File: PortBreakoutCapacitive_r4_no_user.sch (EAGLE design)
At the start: 10 parts, among them IC1 AT42QT1011-TSHR

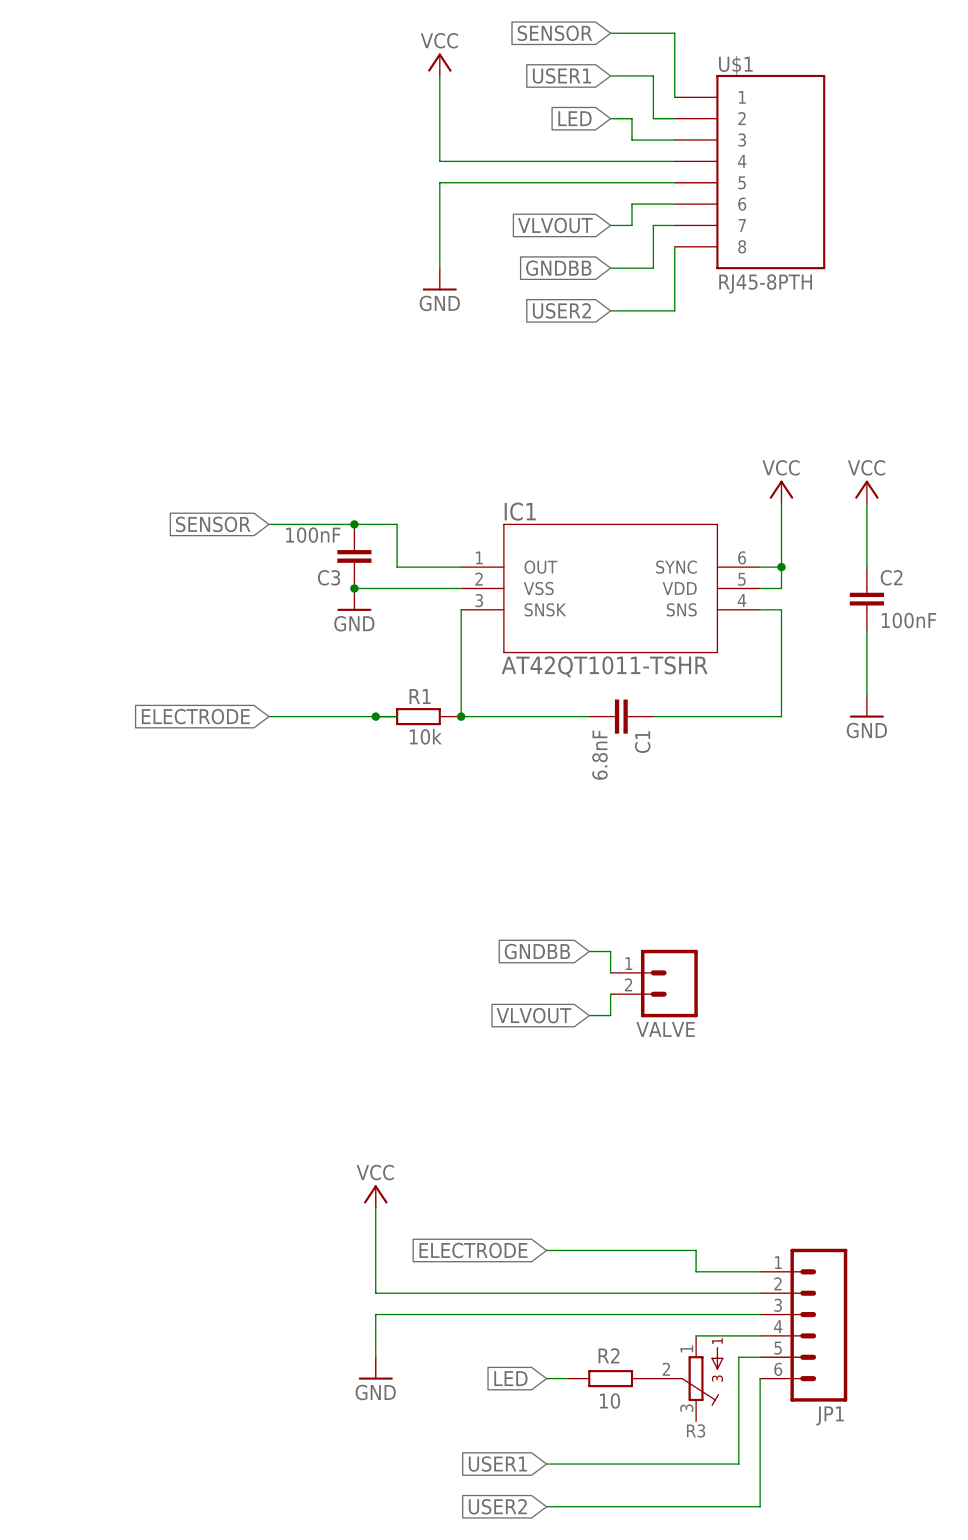
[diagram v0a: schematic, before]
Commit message: rev 4: C1 with lower capacitance
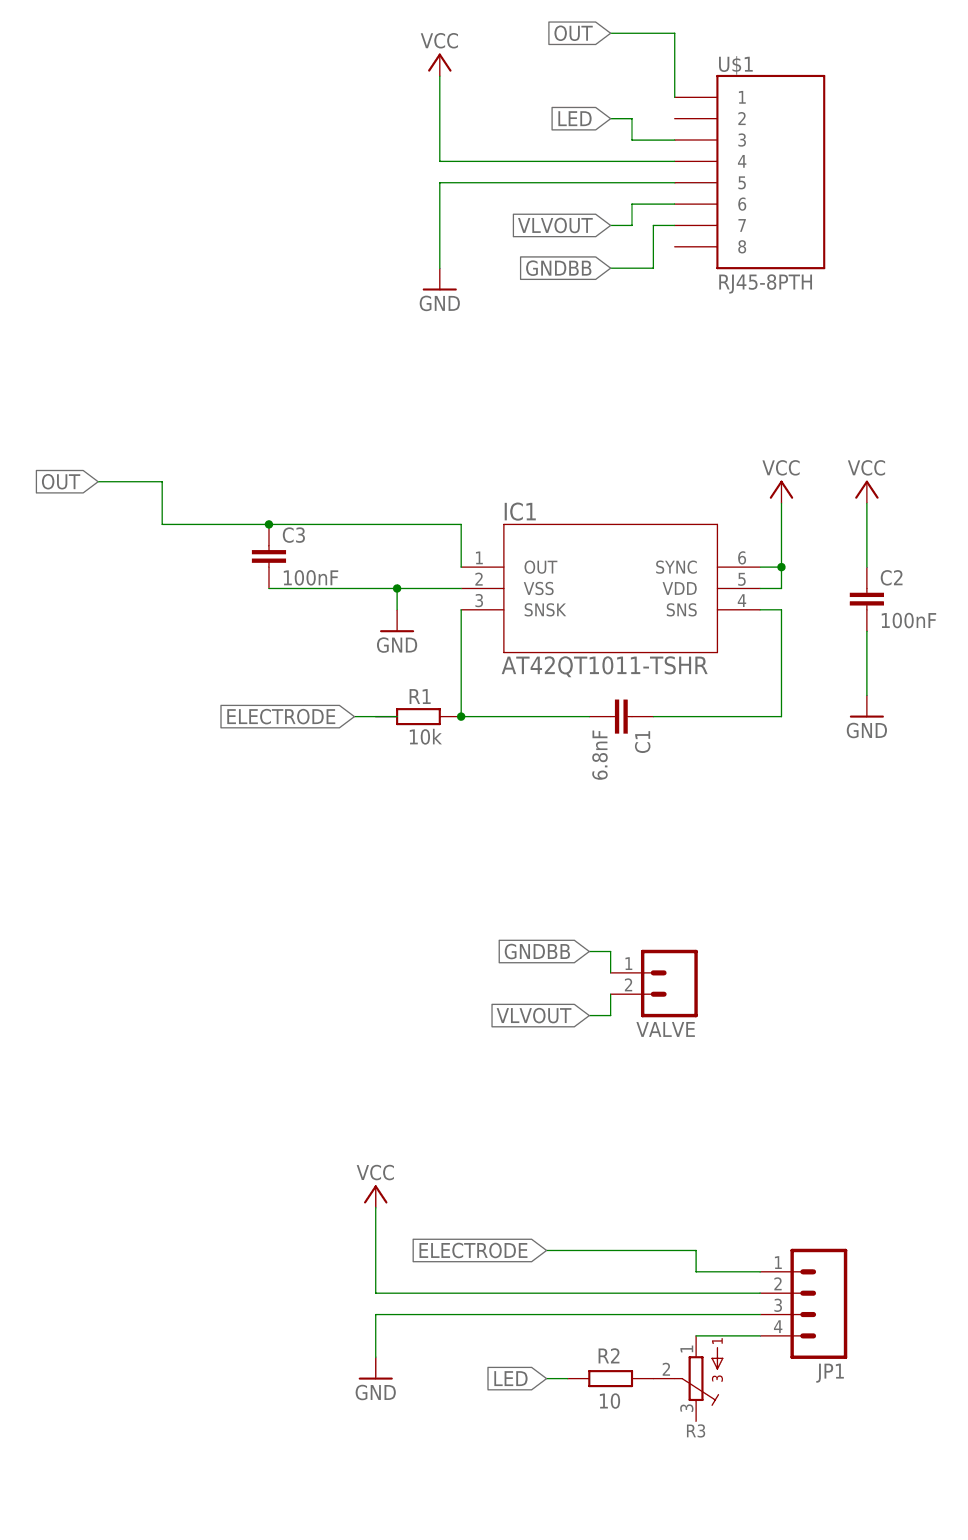
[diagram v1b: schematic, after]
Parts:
- JP1: device SparkFun:M063.5MM-6 -> SparkFun-Connectors:CONN_04SCREW
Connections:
- removed net SENSOR: C3.2, IC1.OUT, U$1.1
- removed net USER1: JP1.5, U$1.2
- removed net USER2: JP1.6, U$1.8
- new net OUT: C3.1, IC1.OUT, U$1.1
- net GND: now also C3.2; no longer C3.1
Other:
- moved on the sheet: C3
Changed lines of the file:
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@@
 <parts>
 <part name="U$1" library="SparkFun" deviceset="RJ45-8" device="PTH"/>
-<part name="JP1" library="SparkFun" deviceset="M06" device="3.5MM-6"/>
+<part name="JP1" library="SparkFun-Connectors" library_urn="urn:adsk.eagle:library:513" deviceset="CONN_04" device="SCREW" package3d_urn="urn:adsk.eagle:package:38090/1"/>
 <part name="VALVE" library="SparkFun" deviceset="M02" device="3.5MM_LOCK"/>
 <part name="R3" library="bourns" deviceset="3362" device="R"/>
@@
 <attribute name="VALUE" x="104.14" y="215.9" size="1.778" layer="95"/>
 </instance>
-<instance part="JP1" gate="G$1" x="114.3" y="93.98" smashed="yes" rot="R180">
-<attribute name="VALUE" x="119.38" y="104.14" size="1.778" layer="96" rot="R180"/>
-<attribute name="NAME" x="119.38" y="83.058" size="1.778" layer="95" rot="R180"/>
+<instance part="JP1" gate="G$1" x="114.3" y="96.52" smashed="yes" rot="R180">
+<attribute name="VALUE" x="119.38" y="106.68" size="1.778" layer="96" rot="R180"/>
+<attribute name="NAME" x="119.38" y="88.138" size="1.778" layer="95" rot="R180"/>
 </instance>
 <instance part="VALVE" gate="G$1" x="99.06" y="134.62" smashed="yes" rot="R180">
@@
 <attribute name="VALUE" x="78.4606" y="170.1546" size="2.0828" layer="96" ratio="6" rot="SR0"/>
 </instance>
-<instance part="GND2" gate="1" x="60.96" y="177.8" smashed="yes">
-<attribute name="VALUE" x="60.96" y="175.26" size="1.778" layer="96" align="bottom-center"/>
+<instance part="GND2" gate="1" x="66.04" y="175.26" smashed="yes">
+<attribute name="VALUE" x="66.04" y="172.72" size="1.778" layer="96" align="bottom-center"/>
 </instance>
 <instance part="P+2" gate="VCC" x="111.76" y="193.04" smashed="yes">
@@
 <attribute name="VALUE" x="63.5" y="111.76" size="1.778" layer="96" align="top-center"/>
 </instance>
-<instance part="C3" gate="G$1" x="60.96" y="182.88" smashed="yes" rot="R180">
-<attribute name="NAME" x="59.436" y="182.499" size="1.778" layer="95" rot="R180"/>
-<attribute name="VALUE" x="59.436" y="187.579" size="1.778" layer="96" rot="R180"/>
+<instance part="C3" gate="G$1" x="50.8" y="185.42" smashed="yes">
+<attribute name="NAME" x="52.324" y="185.801" size="1.778" layer="95"/>
+<attribute name="VALUE" x="52.324" y="180.721" size="1.778" layer="96"/>
 </instance>
 </instances>
@@
 </busses>
 <nets>
-<net name="SENSOR" class="0">
+<net name="OUT" class="0">
 <segment>
 <pinref part="U$1" gate="G$1" pin="1"/>
@@
 </segment>
 <segment>
-<label x="50.8" y="187.96" size="1.778" layer="95" rot="R180" xref="yes"/>
+<label x="30.48" y="193.04" size="1.778" layer="95" rot="R180" xref="yes"/>
+<wire x1="30.48" y1="193.04" x2="38.1" y2="193.04" width="0.1524" layer="91"/>
+<wire x1="38.1" y1="193.04" x2="38.1" y2="187.96" width="0.1524" layer="91"/>
+<pinref part="C3" gate="G$1" pin="1"/>
+<wire x1="38.1" y1="187.96" x2="50.8" y2="187.96" width="0.1524" layer="91"/>
+<wire x1="50.8" y1="187.96" x2="73.66" y2="187.96" width="0.1524" layer="91"/>
+<junction x="50.8" y="187.96"/>
 <pinref part="IC1" gate="A" pin="OUT"/>
-<pinref part="C3" gate="G$1" pin="2"/>
-<wire x1="60.96" y1="187.96" x2="66.04" y2="187.96" width="0.1524" layer="91"/>
-<wire x1="66.04" y1="187.96" x2="66.04" y2="182.88" width="0.1524" layer="91"/>
-<wire x1="66.04" y1="182.88" x2="73.66" y2="182.88" width="0.1524" layer="91"/>
-<wire x1="50.8" y1="187.96" x2="60.96" y2="187.96" width="0.1524" layer="91"/>
-<junction x="60.96" y="187.96"/>
+<wire x1="73.66" y1="187.96" x2="73.66" y2="182.88" width="0.1524" layer="91"/>
 </segment>
 </net>
@@
 <pinref part="IC1" gate="A" pin="VSS"/>
 <pinref part="GND2" gate="1" pin="GND"/>
-<wire x1="73.66" y1="180.34" x2="60.96" y2="180.34" width="0.1524" layer="91"/>
-<pinref part="C3" gate="G$1" pin="1"/>
-<junction x="60.96" y="180.34"/>
+<wire x1="73.66" y1="180.34" x2="66.04" y2="180.34" width="0.1524" layer="91"/>
+<wire x1="66.04" y1="180.34" x2="66.04" y2="177.8" width="0.1524" layer="91"/>
+<pinref part="C3" gate="G$1" pin="2"/>
+<wire x1="50.8" y1="180.34" x2="66.04" y2="180.34" width="0.1524" layer="91"/>
+<junction x="66.04" y="180.34"/>
 </segment>
 <segment>
@@
 </segment>
 </net>
-<net name="USER1" class="0">
-<segment>
-<pinref part="U$1" gate="G$1" pin="2"/>
-<wire x1="99.06" y1="236.22" x2="96.52" y2="236.22" width="0.1524" layer="91"/>
-<wire x1="96.52" y1="236.22" x2="96.52" y2="241.3" width="0.1524" layer="91"/>
-<wire x1="96.52" y1="241.3" x2="91.44" y2="241.3" width="0.1524" layer="91"/>
-<label x="91.44" y="241.3" size="1.778" layer="95" rot="R180" xref="yes"/>
-</segment>
-<segment>
-<pinref part="JP1" gate="G$1" pin="5"/>
-<wire x1="109.22" y1="88.9" x2="106.68" y2="88.9" width="0.1524" layer="91"/>
-<wire x1="106.68" y1="88.9" x2="106.68" y2="76.2" width="0.1524" layer="91"/>
-<wire x1="106.68" y1="76.2" x2="83.82" y2="76.2" width="0.1524" layer="91"/>
-<label x="83.82" y="76.2" size="1.778" layer="95" rot="R180" xref="yes"/>
-</segment>
-</net>
-<net name="USER2" class="0">
-<segment>
-<pinref part="U$1" gate="G$1" pin="8"/>
-<wire x1="99.06" y1="220.98" x2="99.06" y2="213.36" width="0.1524" layer="91"/>
-<wire x1="99.06" y1="213.36" x2="91.44" y2="213.36" width="0.1524" layer="91"/>
-<label x="91.44" y="213.36" size="1.778" layer="95" rot="R180" xref="yes"/>
-</segment>
-<segment>
-<wire x1="83.82" y1="71.12" x2="109.22" y2="71.12" width="0.1524" layer="91"/>
-<wire x1="109.22" y1="71.12" x2="109.22" y2="86.36" width="0.1524" layer="91"/>
-<pinref part="JP1" gate="G$1" pin="6"/>
-<label x="83.82" y="71.12" size="1.778" layer="95" rot="R180" xref="yes"/>
-</segment>
-</net>
 <net name="SNS" class="0">
 <segment>
@@
 <segment>
 <wire x1="63.5" y1="165.1" x2="66.04" y2="165.1" width="0.1524" layer="91"/>
-<label x="50.8" y="165.1" size="1.778" layer="95" rot="R180" xref="yes"/>
+<wire x1="63.5" y1="165.1" x2="60.96" y2="165.1" width="0.1524" layer="91"/>
+<label x="60.96" y="165.1" size="1.778" layer="95" rot="R180" xref="yes"/>
 <pinref part="R1" gate="G$1" pin="1"/>
-<wire x1="50.8" y1="165.1" x2="63.5" y2="165.1" width="0.1524" layer="91"/>
-<junction x="63.5" y="165.1"/>
 </segment>
 </net>
@@
 </sheet>
 </sheets>
+<errors>
+</errors>
 </schematic>
 </drawing>

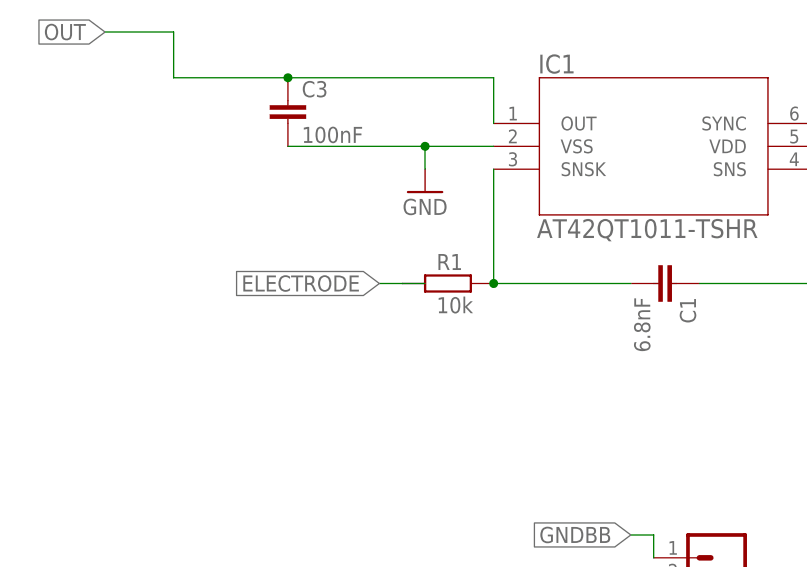
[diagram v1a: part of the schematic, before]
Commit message: some changes to trace routing
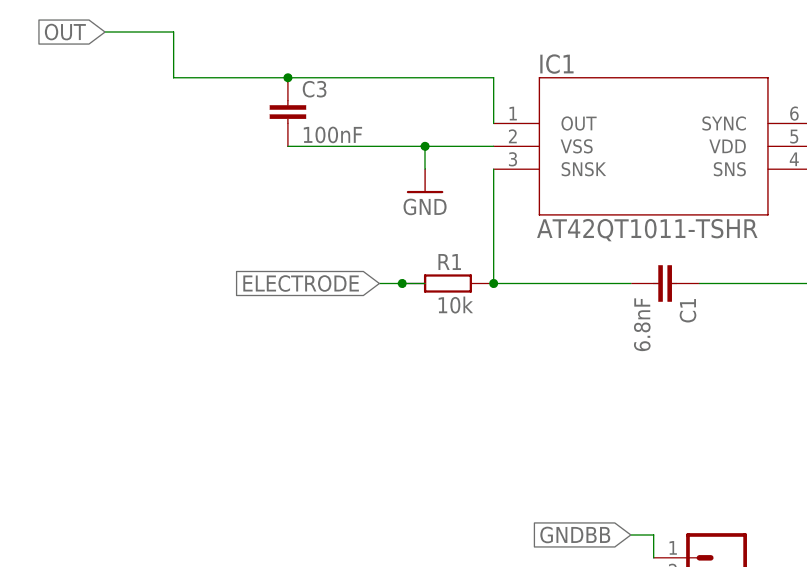
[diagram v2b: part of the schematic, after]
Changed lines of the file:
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@@
 <label x="60.96" y="165.1" size="1.778" layer="95" rot="R180" xref="yes"/>
 <pinref part="R1" gate="G$1" pin="1"/>
+<junction x="63.5" y="165.1"/>
 </segment>
 </net>
@@
 </sheet>
 </sheets>
-<errors>
-</errors>
 </schematic>
 </drawing>
